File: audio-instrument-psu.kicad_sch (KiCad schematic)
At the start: 46 parts, among them J1 Molex_SL_01x04_Male, J2 Molex_SL_01x04_Male, J3 Molex_SL_01x04_Male, J4 Molex_SL_01x04_Male, J5 Molex_SL_01x04_Male, J99 Mini-DIN-4, U1 LM317_TO-220, U2 LM337_TO220

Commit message: change board to attach to heatsink mounting holes
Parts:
- H1, H2: value MountingHole_Pad -> MountingHole; footprint Mounting_gkeeth:MountingBracket_Keystone_4335_Width12.7mm_Drill3.05mm -> MountingHole:MountingHole_4.3mm_M4; symbol Mechanical:MountingHole_Pad -> Mechanical:MountingHole; Manufacturer Keystone -> (none); Manufacturer PN 4335 -> (none)
- H3: footprint MountingHole:MountingHole_3.2mm_M3_Pad -> MountingHole:MountingHole_4.3mm_M4_Pad
- H4: value MountingHole_Pad -> MountingHole; footprint MountingHole:MountingHole_3.2mm_M3_Pad -> MountingHole:MountingHole_4.3mm_M4; symbol Mechanical:MountingHole_Pad -> Mechanical:MountingHole; now in the parts list
- U1, U2: footprint Package_TO_SOT_THT:TO-220-3_Vertical -> Package_TO_SOT_THT:TO-220-3_Horizontal_TabUp
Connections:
- net 12VAC_unfused: now also J1.3 (Pin_3), J1.4 (Pin_4); no longer J1.1 (Pin_1), J1.2 (Pin_2)
- net GND: now also J1.1 (Pin_1), J1.2 (Pin_2); no longer H1.1, H2.1, H4.1, J1.3 (Pin_3), J1.4 (Pin_4)
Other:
- note added: "M4 standoffs"

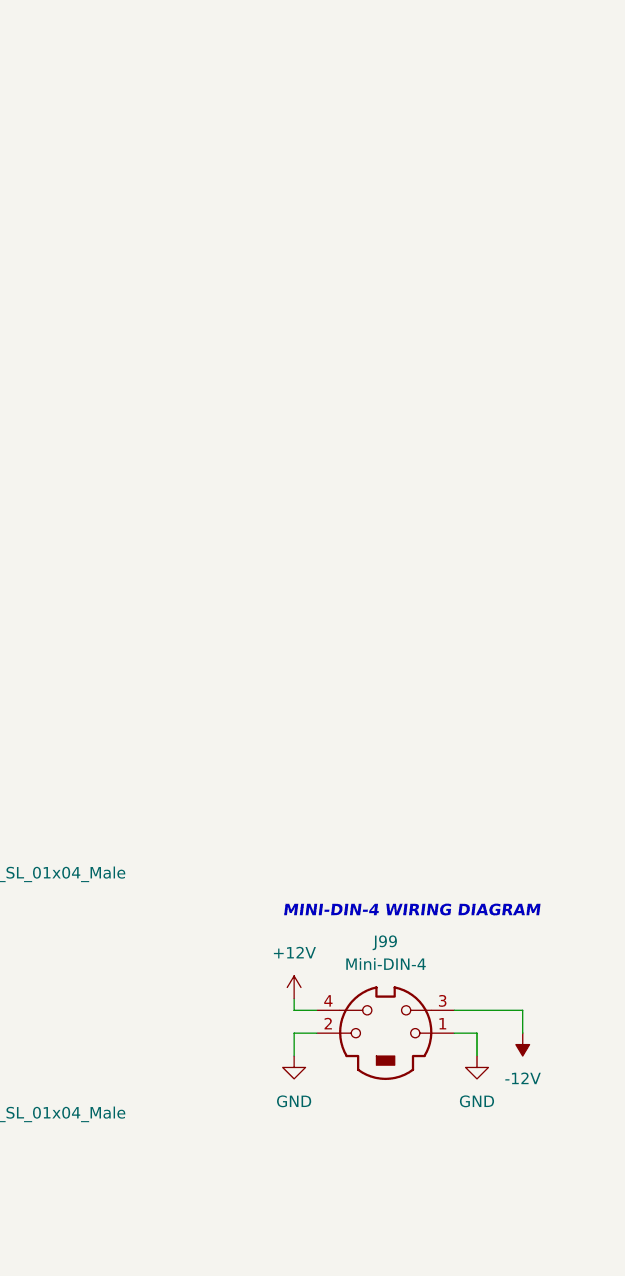
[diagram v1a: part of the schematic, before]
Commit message: add power-din pinout to schematic
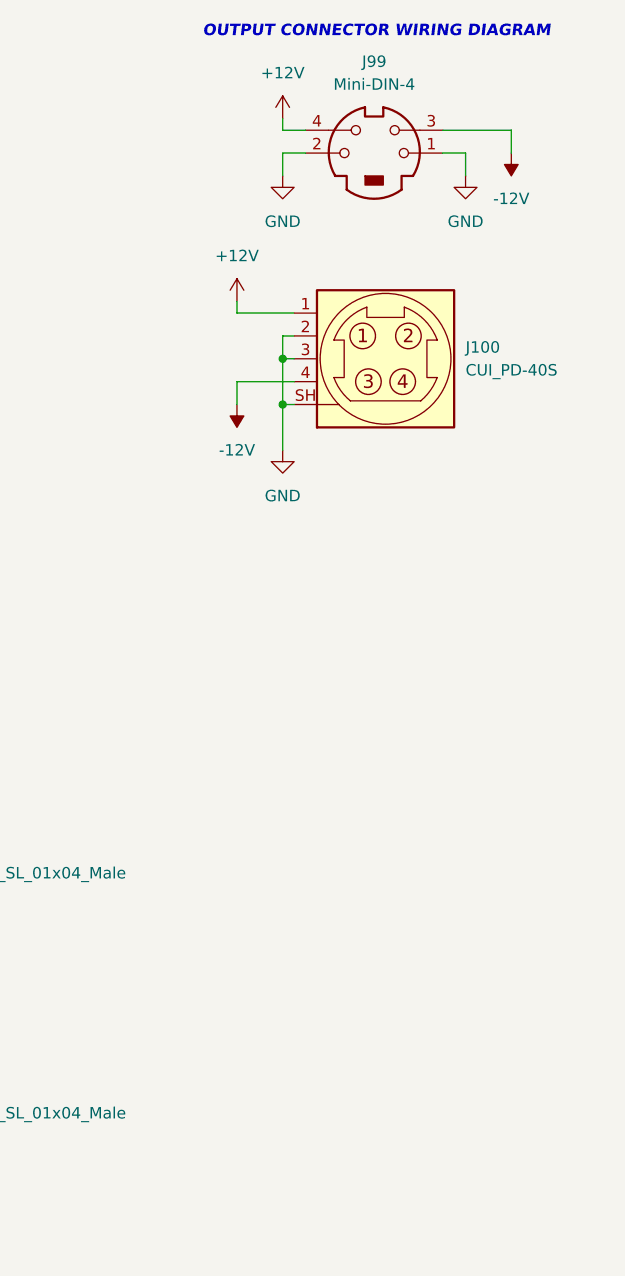
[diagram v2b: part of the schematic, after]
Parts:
- added J100: CUI_PD-40S, Connector_Mini_DIN_gkeeth:Power-DIN_CUI_PD-40S_Horizontal, symbol Connector_gkeeth:CUI_PD-40S
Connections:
- net +12V: now also J100.1
- net -12V: now also J100.4 (Shield)
- net GND: now also J100.2, J100.3, J100.SH (Shield)
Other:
- note added: "OUTPUT CONNECTOR WIRING DIAGRAM"
- note removed: "MINI-DIN-4 WIRING DIAGRAM"
- moved on the sheet: J99
